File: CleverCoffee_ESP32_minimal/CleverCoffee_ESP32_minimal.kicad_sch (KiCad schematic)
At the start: 23 parts

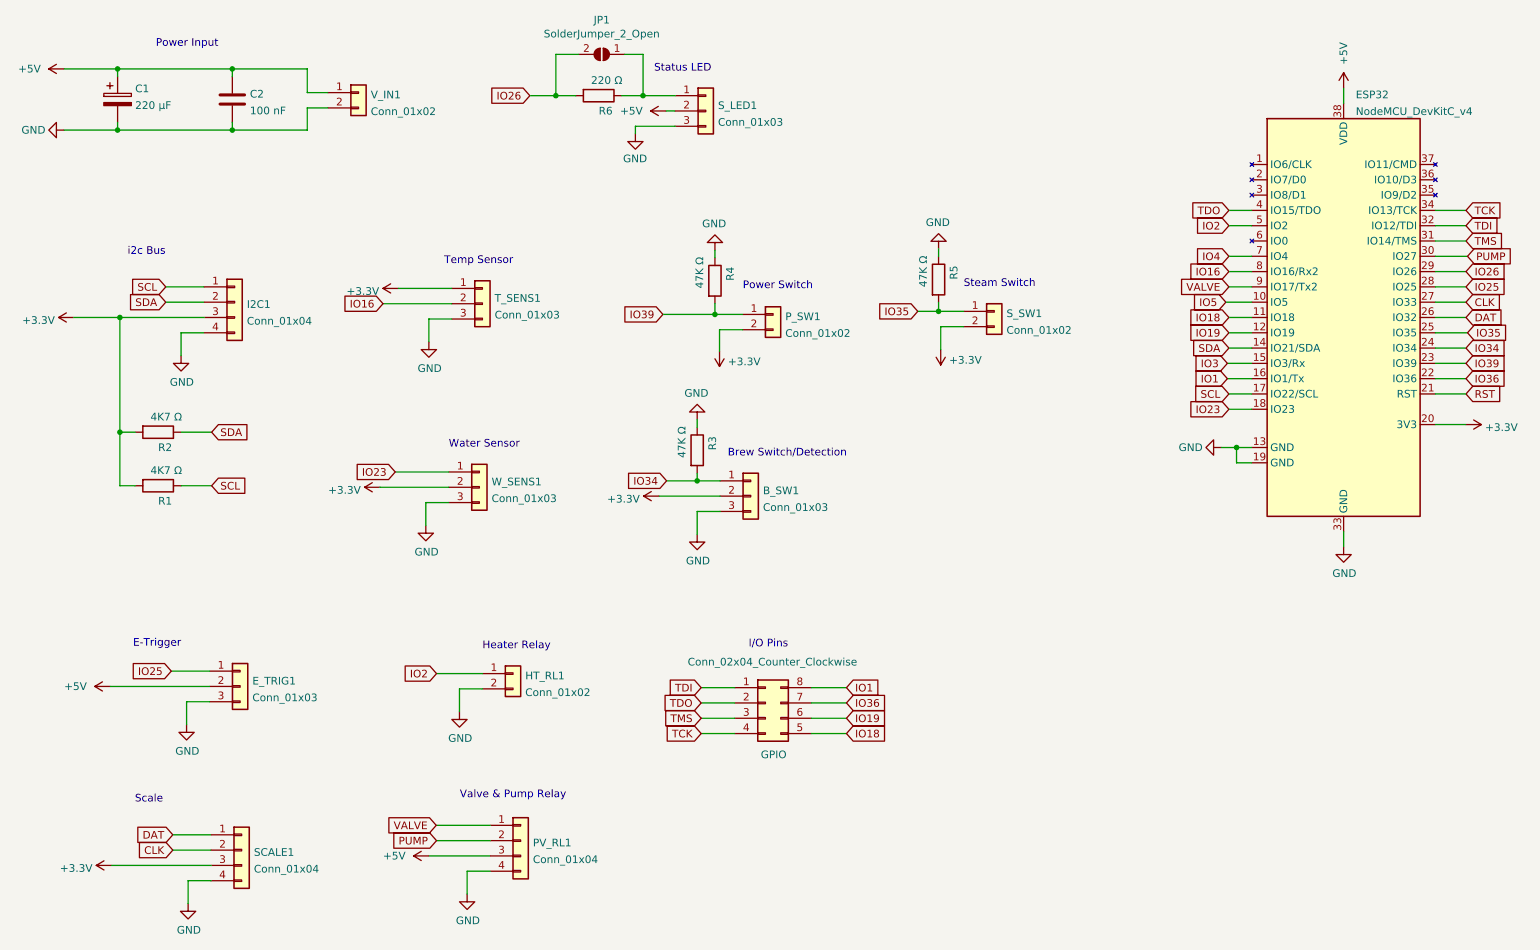
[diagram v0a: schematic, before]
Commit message: Bugfix Labels Silkscreen
S_LED change VCC to 5V
E_TRIG change VCC to 5V
W_SENS change IO36 to IO23
GPIO change IO23 to IO36
change all VCC to 3,3V
change GPIO to IO Nummer
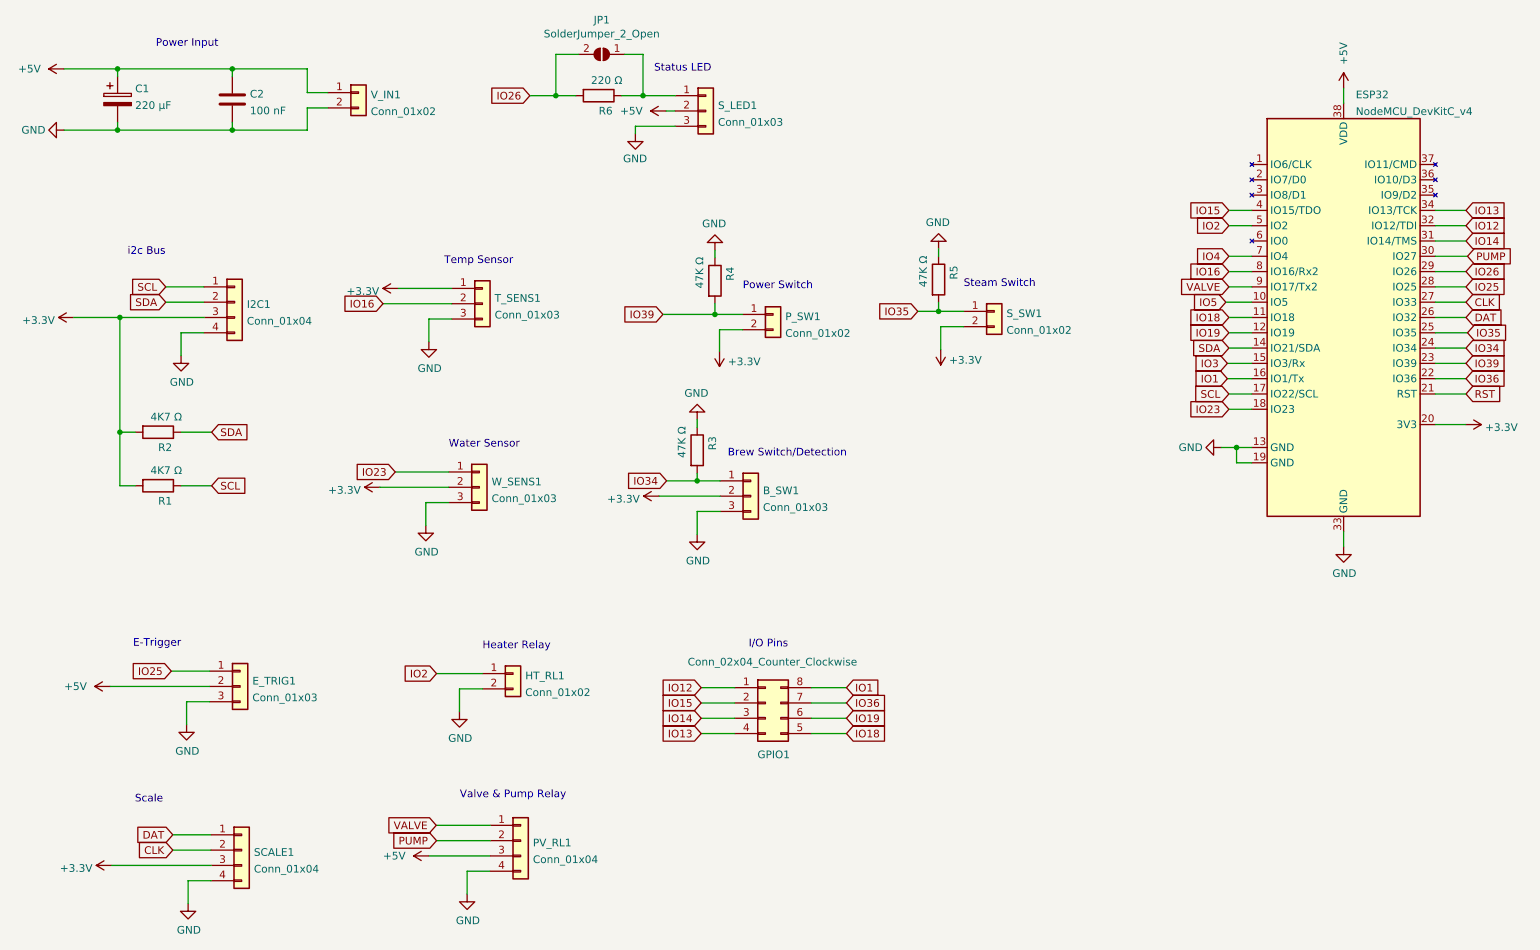
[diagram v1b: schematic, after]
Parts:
- renumbered GPIO to GPIO1
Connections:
- net TCK renamed IO13
- net TDI renamed IO12
- net TDO renamed IO15
- net TMS renamed IO14
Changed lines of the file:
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@@
   (title_block
     (title "ESP32 Breakout Board - Minimal")
-    (date "2023-01-29")
-    (rev "1.2")
+    (date "2023-02-20")
+    (rev "1.3")
     (company "CleverCoffee ")
   )
@@
     (effects (font (size 1.27 1.27)) (justify left bottom))
   )
-  (global_label "TDO" (shape input) (at 139.7 130.048 180) (fields_autoplaced)
-    (effects (font (size 1.27 1.27)) (justify right))
-    (property "Intersheet References" "${INTERSHEET_REFS}" (id 0) (at 389.89 206.248 0)
-      (effects (font (size 1.27 1.27)) hide)
+  (global_label "IO15" (shape input) (at 139.7 130.048 180) (fields_autoplaced)
+    (effects (font (size 1.27 1.27)) (justify right))
+    (property "Intersheet References" "${INTERSHEET_REFS}" (id 0) (at 132.9326 129.9686 0)
+      (effects (font (size 1.27 1.27)) (justify right) hide)
     )
   )
@@
     )
   )
-  (global_label "TDI" (shape input) (at 139.7 127.508 180) (fields_autoplaced)
-    (effects (font (size 1.27 1.27)) (justify right))
-    (property "Intersheet References" "${INTERSHEET_REFS}" (id 0) (at 389.89 206.248 0)
-      (effects (font (size 1.27 1.27)) hide)
+  (global_label "IO12" (shape input) (at 139.7 127.508 180) (fields_autoplaced)
+    (effects (font (size 1.27 1.27)) (justify right))
+    (property "Intersheet References" "${INTERSHEET_REFS}" (id 0) (at 132.9326 127.4286 0)
+      (effects (font (size 1.27 1.27)) (justify right) hide)
     )
   )
@@
     )
   )
-  (global_label "TDI" (shape input) (at 266.7 50.8 0) (fields_autoplaced)
-    (effects (font (size 1.27 1.27)) (justify left))
-    (property "Intersheet References" "${INTERSHEET_REFS}" (id 0) (at 16.51 -27.94 0)
-      (effects (font (size 1.27 1.27)) hide)
+  (global_label "IO12" (shape input) (at 266.7 50.8 0) (fields_autoplaced)
+    (effects (font (size 1.27 1.27)) (justify left))
+    (property "Intersheet References" "${INTERSHEET_REFS}" (id 0) (at 273.4674 50.7206 0)
+      (effects (font (size 1.27 1.27)) (justify left) hide)
     )
   )
@@
     )
   )
-  (global_label "TDO" (shape input) (at 227.33 48.26 180) (fields_autoplaced)
-    (effects (font (size 1.27 1.27)) (justify right))
-    (property "Intersheet References" "${INTERSHEET_REFS}" (id 0) (at 477.52 124.46 0)
-      (effects (font (size 1.27 1.27)) hide)
+  (global_label "IO15" (shape input) (at 227.33 48.26 180) (fields_autoplaced)
+    (effects (font (size 1.27 1.27)) (justify right))
+    (property "Intersheet References" "${INTERSHEET_REFS}" (id 0) (at 220.5626 48.1806 0)
+      (effects (font (size 1.27 1.27)) (justify right) hide)
     )
   )
@@
     )
   )
-  (global_label "TMS" (shape input) (at 139.7 132.588 180) (fields_autoplaced)
-    (effects (font (size 1.27 1.27)) (justify right))
-    (property "Intersheet References" "${INTERSHEET_REFS}" (id 0) (at 389.89 206.248 0)
-      (effects (font (size 1.27 1.27)) hide)
+  (global_label "IO14" (shape input) (at 139.7 132.588 180) (fields_autoplaced)
+    (effects (font (size 1.27 1.27)) (justify right))
+    (property "Intersheet References" "${INTERSHEET_REFS}" (id 0) (at 132.9326 132.5086 0)
+      (effects (font (size 1.27 1.27)) (justify right) hide)
     )
   )
@@
     )
   )
-  (global_label "TCK" (shape input) (at 266.7 48.26 0) (fields_autoplaced)
-    (effects (font (size 1.27 1.27)) (justify left))
-    (property "Intersheet References" "${INTERSHEET_REFS}" (id 0) (at 16.51 -22.86 0)
-      (effects (font (size 1.27 1.27)) hide)
+  (global_label "IO13" (shape input) (at 266.7 48.26 0) (fields_autoplaced)
+    (effects (font (size 1.27 1.27)) (justify left))
+    (property "Intersheet References" "${INTERSHEET_REFS}" (id 0) (at 273.4674 48.1806 0)
+      (effects (font (size 1.27 1.27)) (justify left) hide)
     )
   )
@@
     )
   )
-  (global_label "TCK" (shape input) (at 139.7 135.128 180) (fields_autoplaced)
-    (effects (font (size 1.27 1.27)) (justify right))
-    (property "Intersheet References" "${INTERSHEET_REFS}" (id 0) (at 389.89 206.248 0)
-      (effects (font (size 1.27 1.27)) hide)
+  (global_label "IO13" (shape input) (at 139.7 135.128 180) (fields_autoplaced)
+    (effects (font (size 1.27 1.27)) (justify right))
+    (property "Intersheet References" "${INTERSHEET_REFS}" (id 0) (at 132.9326 135.0486 0)
+      (effects (font (size 1.27 1.27)) (justify right) hide)
     )
   )
@@
     )
   )
-  (global_label "TMS" (shape input) (at 266.7 53.34 0) (fields_autoplaced)
-    (effects (font (size 1.27 1.27)) (justify left))
-    (property "Intersheet References" "${INTERSHEET_REFS}" (id 0) (at 16.51 -20.32 0)
-      (effects (font (size 1.27 1.27)) hide)
+  (global_label "IO14" (shape input) (at 266.7 53.34 0) (fields_autoplaced)
+    (effects (font (size 1.27 1.27)) (justify left))
+    (property "Intersheet References" "${INTERSHEET_REFS}" (id 0) (at 273.4674 53.2606 0)
+      (effects (font (size 1.27 1.27)) (justify left) hide)
     )
   )
@@
   (symbol (lib_id "Connector_Generic:Conn_02x04_Counter_Clockwise") (at 150.368 130.048 0) (unit 1)
     (in_bom yes) (on_board yes)
-    (property "Reference" "GPIO" (id 0) (at 151.7396 138.6332 0))
+    (property "Reference" "GPIO1" (id 0) (at 151.7396 138.6332 0))
     (property "Value" "Conn_02x04_Counter_Clockwise" (id 1) (at 151.5364 123.2408 0))
     (property "Footprint" "Connector_PinSocket_2.54mm:PinSocket_2x04_P2.54mm_Vertical" (id 2) (at 156.0068 141.6304 0)
@@
     )
     (path "/95c6b157-c871-406b-9357-d6d62a988028"
-      (reference "GPIO") (unit 1) (value "Conn_02x04_Counter_Clockwise") (footprint "Connector_PinSocket_2.54mm:PinSocket_2x04_P2.54mm_Vertical")
+      (reference "GPIO1") (unit 1) (value "Conn_02x04_Counter_Clockwise") (footprint "Connector_PinSocket_2.54mm:PinSocket_2x04_P2.54mm_Vertical")
     )
     (path "/1001235b-c68f-444b-a75c-21c500a50d69"
